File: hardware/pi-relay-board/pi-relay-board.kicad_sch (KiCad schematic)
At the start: 1 part, among them J1 Raspberry_Pi_2_3

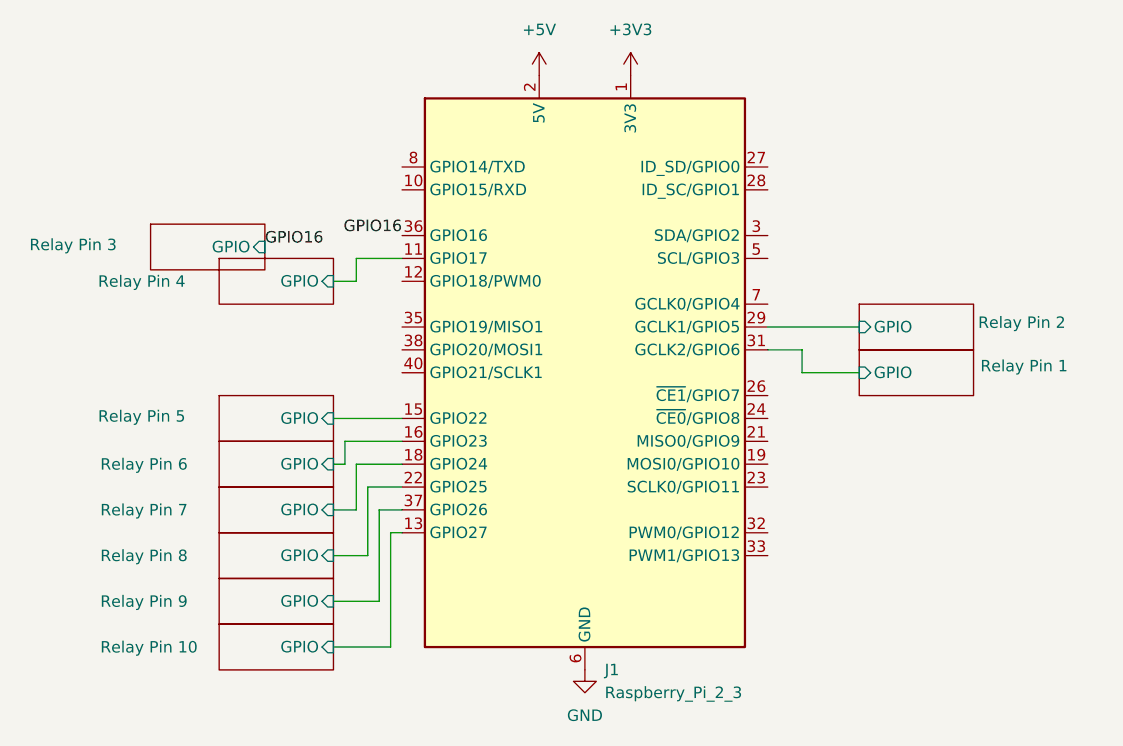
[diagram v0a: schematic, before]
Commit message: hardware: change to tht
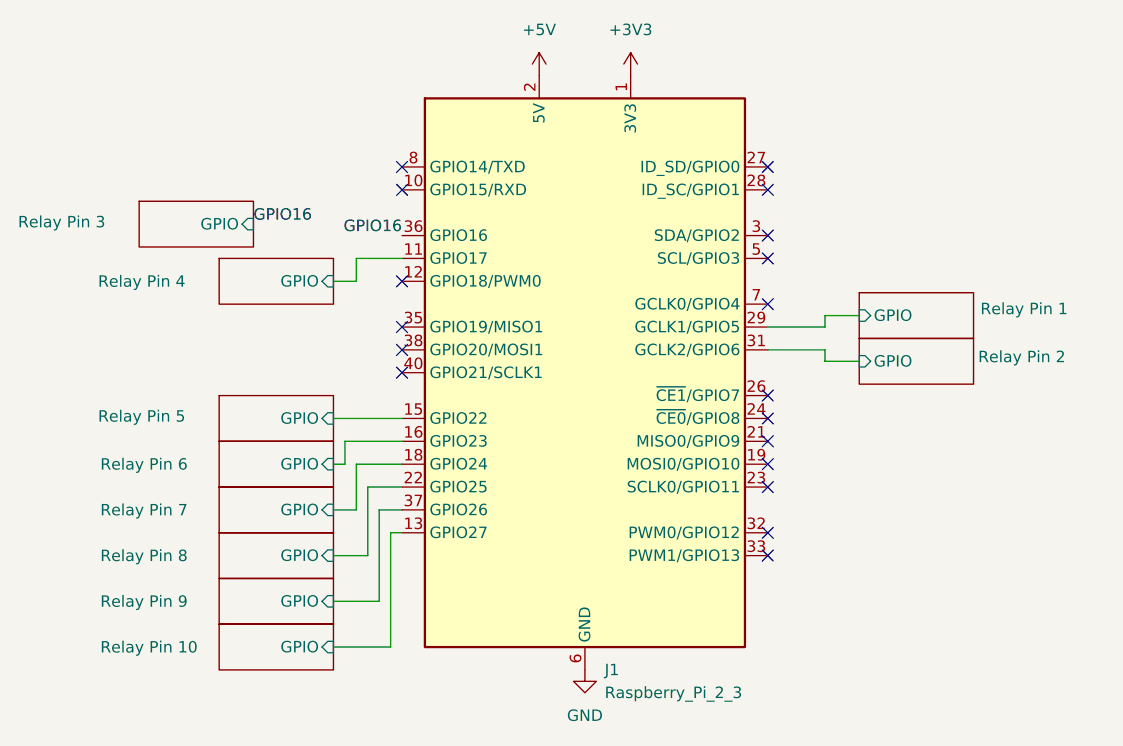
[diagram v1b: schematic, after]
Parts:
- J1: footprint custom:Raspberry Connector -> Connector_PinHeader_2.54mm:PinHeader_2x20_P2.54mm_Vertical
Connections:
- net Relay Pin 1/GPIO: now also J1.29 (GCLK1/GPIO5); no longer J1.31 (GCLK2/GPIO6)
- net Relay Pin 2/GPIO: now also J1.31 (GCLK2/GPIO6); no longer J1.29 (GCLK1/GPIO5)
- no-connect marks 0 -> 18
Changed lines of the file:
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@@
 	(generator_version "8.0")
 	(paper "A4")
+	(no_connect
+		(at 73.66 88.9)
+	)
+	(no_connect
+		(at 114.3 68.58)
+	)
+	(no_connect
+		(at 114.3 78.74)
+	)
+	(no_connect
+		(at 114.3 109.22)
+	)
+	(no_connect
+		(at 73.66 71.12)
+	)
+	(no_connect
+		(at 114.3 104.14)
+	)
+	(no_connect
+		(at 114.3 83.82)
+	)
+	(no_connect
+		(at 73.66 91.44)
+	)
+	(no_connect
+		(at 114.3 76.2)
+	)
+	(no_connect
+		(at 114.3 101.6)
+	)
+	(no_connect
+		(at 73.66 68.58)
+	)
+	(no_connect
+		(at 73.66 81.28)
+	)
+	(no_connect
+		(at 114.3 111.76)
+	)
+	(no_connect
+		(at 114.3 99.06)
+	)
+	(no_connect
+		(at 114.3 96.52)
+	)
+	(no_connect
+		(at 114.3 93.98)
+	)
+	(no_connect
+		(at 73.66 86.36)
+	)
+	(no_connect
+		(at 114.3 71.12)
+	)
 	(wire
 		(pts
@@
 	(wire
 		(pts
-			(xy 118.11 88.9) (xy 114.3 88.9)
+			(xy 120.65 88.9) (xy 120.65 90.17)
+		)
+		(stroke
+			(width 0)
+			(type default)
+		)
+	)
+	(wire
+		(pts
+			(xy 120.65 86.36) (xy 120.65 85.09)
 		)
 		(stroke
@@
 	(wire
 		(pts
-			(xy 124.46 91.44) (xy 118.11 91.44)
-		)
-		(stroke
-			(width 0)
-			(type default)
-		)
-	)
-	(wire
-		(pts
 			(xy 72.39 121.92) (xy 72.39 109.22)
 		)
@@
 	(wire
 		(pts
+			(xy 120.65 85.09) (xy 124.46 85.09)
+		)
+		(stroke
+			(width 0)
+			(type default)
+		)
+	)
+	(wire
+		(pts
+			(xy 114.3 88.9) (xy 120.65 88.9)
+		)
+		(stroke
+			(width 0)
+			(type default)
+		)
+	)
+	(wire
+		(pts
 			(xy 68.58 81.28) (xy 68.58 78.74)
 		)
@@
 	(wire
 		(pts
+			(xy 114.3 86.36) (xy 120.65 86.36)
+		)
+		(stroke
+			(width 0)
+			(type default)
+		)
+	)
+	(wire
+		(pts
 			(xy 67.31 101.6) (xy 67.31 99.06)
 		)
@@
 	(wire
 		(pts
-			(xy 114.3 86.36) (xy 124.46 86.36)
-		)
-		(stroke
-			(width 0)
-			(type default)
-		)
-	)
-	(wire
-		(pts
-			(xy 118.11 91.44) (xy 118.11 88.9)
+			(xy 120.65 90.17) (xy 124.46 90.17)
 		)
 		(stroke
@@
 	)
 	(label "GPIO16"
-		(at 58.42 77.47 0)
+		(at 57.15 74.93 0)
 		(fields_autoplaced yes)
 		(effects
@@
 			)
 		)
-		(property "Footprint" "custom:Raspberry Connector"
+		(property "Footprint" "Connector_PinHeader_2.54mm:PinHeader_2x20_P2.54mm_Vertical"
 			(at 93.98 91.44 0)
 			(effects
@@
 	)
 	(sheet
-		(at 45.72 74.93)
+		(at 44.45 72.39)
 		(size 12.7 5.08)
 		(stroke
@@
 		)
 		(property "Sheetname" "Relay Pin 3"
-			(at 32.258 77.978 0)
+			(at 30.988 75.438 0)
 			(effects
 				(font
@@
 		)
 		(property "Sheetfile" "relay_pin.kicad_sch"
-			(at 45.72 80.5946 0)
+			(at 44.45 78.0546 0)
 			(effects
 				(font
@@
 		)
 		(pin "GPIO" input
-			(at 58.42 77.47 0)
+			(at 57.15 74.93 0)
 			(effects
 				(font
@@
 	)
 	(sheet
-		(at 124.46 88.9)
+		(at 124.46 82.55)
 		(size 12.7 5.08)
 		(stroke
@@
 		)
 		(property "Sheetname" "Relay Pin 1"
-			(at 137.922 91.44 0)
+			(at 137.922 85.09 0)
 			(effects
 				(font
@@
 		)
 		(property "Sheetfile" "relay_pin.kicad_sch"
-			(at 124.46 94.5646 0)
+			(at 124.46 88.2146 0)
 			(effects
 				(font
@@
 		)
 		(pin "GPIO" input
-			(at 124.46 91.44 180)
+			(at 124.46 85.09 180)
 			(effects
 				(font
@@
 	)
 	(sheet
-		(at 124.46 83.82)
+		(at 124.46 87.63)
 		(size 12.7 5.08)
 		(stroke
@@
 		)
 		(property "Sheetname" "Relay Pin 2"
-			(at 137.668 86.614 0)
+			(at 137.668 90.424 0)
 			(effects
 				(font
@@
 		)
 		(property "Sheetfile" "relay_pin.kicad_sch"
-			(at 124.46 89.4846 0)
+			(at 124.46 93.2946 0)
 			(effects
 				(font
@@
 		)
 		(pin "GPIO" input
-			(at 124.46 86.36 180)
-			(effects
-				(font
+			(at 124.46 90.17 180)
+			(effects
+				(font

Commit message: feat: pcb bc547 footprint, laser image
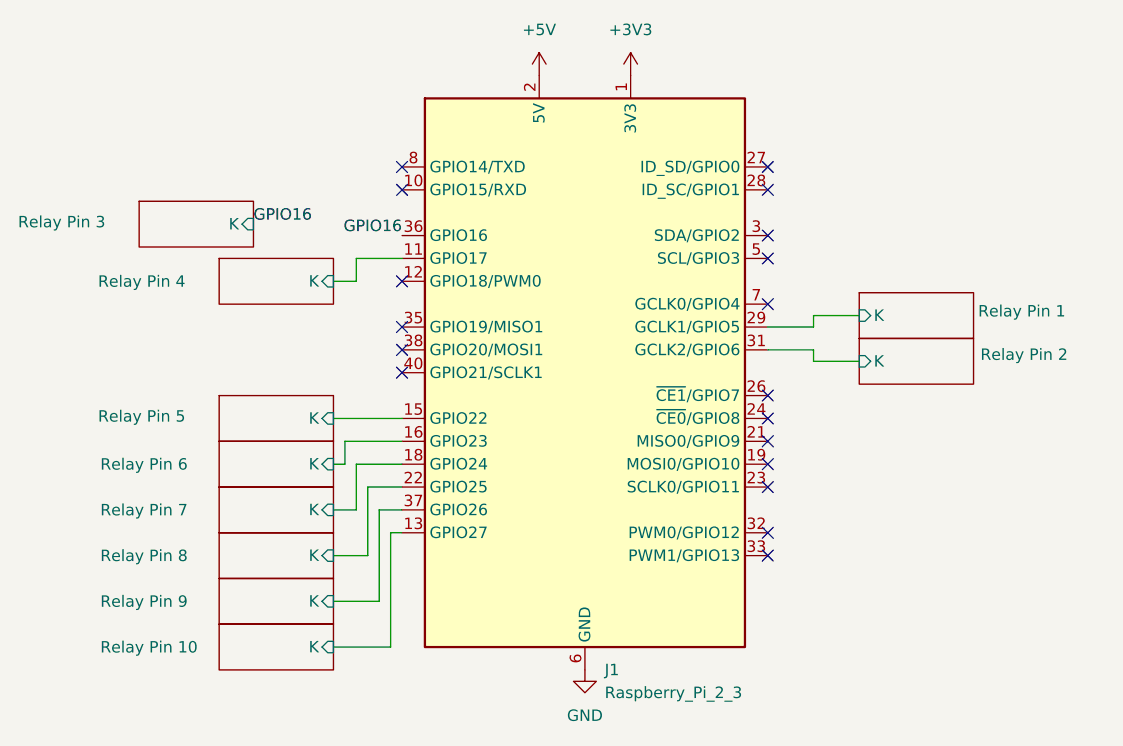
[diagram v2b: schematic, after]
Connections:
- net Relay Pin 1/GPIO renamed Relay Pin 1/K
- net Relay Pin 10/GPIO renamed Relay Pin 10/K
- net Relay Pin 2/GPIO renamed Relay Pin 2/K
- net Relay Pin 4/GPIO renamed Relay Pin 4/K
- net Relay Pin 5/GPIO renamed Relay Pin 5/K
- net Relay Pin 6/GPIO renamed Relay Pin 6/K
- net Relay Pin 7/GPIO renamed Relay Pin 7/K
- net Relay Pin 8/GPIO renamed Relay Pin 8/K
- net Relay Pin 9/GPIO renamed Relay Pin 9/K
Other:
- sheet Relay Pin 1 ports: added K; removed GPIO
- sheet Relay Pin 10 ports: added K; removed GPIO
- sheet Relay Pin 2 ports: added K; removed GPIO
- sheet Relay Pin 3 ports: added K; removed GPIO
- sheet Relay Pin 4 ports: added K; removed GPIO
- sheet Relay Pin 5 ports: added K; removed GPIO
- sheet Relay Pin 6 ports: added K; removed GPIO
- sheet Relay Pin 7 ports: added K; removed GPIO
- sheet Relay Pin 8 ports: added K; removed GPIO
- sheet Relay Pin 9 ports: added K; removed GPIO
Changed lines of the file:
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@@
 	(wire
 		(pts
-			(xy 120.65 88.9) (xy 120.65 90.17)
-		)
-		(stroke
-			(width 0)
-			(type default)
-		)
-	)
-	(wire
-		(pts
-			(xy 120.65 86.36) (xy 120.65 85.09)
+			(xy 119.38 88.9) (xy 119.38 90.17)
 		)
 		(stroke
@@
 	(wire
 		(pts
+			(xy 119.38 85.09) (xy 124.46 85.09)
+		)
+		(stroke
+			(width 0)
+			(type default)
+		)
+	)
+	(wire
+		(pts
 			(xy 72.39 121.92) (xy 72.39 109.22)
 		)
@@
 	(wire
 		(pts
-			(xy 120.65 85.09) (xy 124.46 85.09)
-		)
-		(stroke
-			(width 0)
-			(type default)
-		)
-	)
-	(wire
-		(pts
-			(xy 114.3 88.9) (xy 120.65 88.9)
+			(xy 119.38 86.36) (xy 114.3 86.36)
+		)
+		(stroke
+			(width 0)
+			(type default)
+		)
+	)
+	(wire
+		(pts
+			(xy 119.38 85.09) (xy 119.38 86.36)
 		)
 		(stroke
@@
 	(wire
 		(pts
-			(xy 114.3 86.36) (xy 120.65 86.36)
-		)
-		(stroke
-			(width 0)
-			(type default)
-		)
-	)
-	(wire
-		(pts
 			(xy 67.31 101.6) (xy 67.31 99.06)
 		)
@@
 	(wire
 		(pts
-			(xy 120.65 90.17) (xy 124.46 90.17)
+			(xy 114.3 88.9) (xy 119.38 88.9)
 		)
 		(stroke
@@
 		(pts
 			(xy 66.04 116.84) (xy 71.12 116.84)
+		)
+		(stroke
+			(width 0)
+			(type default)
+		)
+	)
+	(wire
+		(pts
+			(xy 119.38 90.17) (xy 124.46 90.17)
 		)
 		(stroke
@@
 			)
 		)
-		(pin "GPIO" input
+		(pin "K" input
 			(at 66.04 106.68 0)
 			(effects
@@
 			)
 		)
-		(pin "GPIO" input
+		(pin "K" input
 			(at 66.04 101.6 0)
 			(effects
@@
 			)
 		)
-		(pin "GPIO" input
+		(pin "K" input
 			(at 57.15 74.93 0)
 			(effects
@@
 			)
 		)
-		(pin "GPIO" input
+		(pin "K" input
 			(at 66.04 81.28 0)
 			(effects
@@
 			)
 		)
-		(pin "GPIO" input
+		(pin "K" input
 			(at 66.04 96.52 0)
 			(effects
@@
 				(path "/d2fef91f-5840-4773-b01e-415a95bac3ff"
 					(page "6")
+				)
+			)
+		)
+	)
+	(sheet
+		(at 124.46 87.63)
+		(size 12.7 5.08)
+		(stroke
+			(width 0.1524)
+			(type solid)
+		)
+		(fill
+			(color 0 0 0 0.0000)
+		)
+		(property "Sheetname" "Relay Pin 2"
+			(at 137.922 90.17 0)
+			(effects
+				(font
+					(size 1.27 1.27)
+				)
+				(justify left bottom)
+			)
+		)
+		(property "Sheetfile" "relay_pin.kicad_sch"
+			(at 124.46 93.2946 0)
+			(effects
+				(font
+					(size 1.27 1.27)
+				)
+				(justify left top)
+				(hide yes)
+			)
+		)
+		(pin "K" input
+			(at 124.46 90.17 180)
+			(effects
+				(font
+					(size 1.27 1.27)
+				)
+				(justify left)
+			)
+		)
+		(instances
+			(project "pi-relay-board"
+				(path "/d2fef91f-5840-4773-b01e-415a95bac3ff"
+					(page "2")
+				)
+			)
+		)
+	)
+	(sheet
+		(at 53.34 114.3)
+		(size 12.7 5.08)
+		(stroke
+			(width 0.1524)
+			(type solid)
+		)
+		(fill
+			(color 0 0 0 0.0000)
+		)
+		(property "Sheetname" "Relay Pin 9"
+			(at 40.132 117.602 0)
+			(effects
+				(font
+					(size 1.27 1.27)
+				)
+				(justify left bottom)
+			)
+		)
+		(property "Sheetfile" "relay_pin.kicad_sch"
+			(at 53.34 119.9646 0)
+			(effects
+				(font
+					(size 1.27 1.27)
+				)
+				(justify left top)
+				(hide yes)
+			)
+		)
+		(pin "K" input
+			(at 66.04 116.84 0)
+			(effects
+				(font
+					(size 1.27 1.27)
+				)
+				(justify right)
+			)
+		)
+		(instances
+			(project "pi-relay-board"
+				(path "/d2fef91f-5840-4773-b01e-415a95bac3ff"
+					(page "10")
+				)
+			)
+		)
+	)
+	(sheet
+		(at 53.34 109.22)
+		(size 12.7 5.08)
+		(stroke
+			(width 0.1524)
+			(type solid)
+		)
+		(fill
+			(color 0 0 0 0.0000)
+		)
+		(property "Sheetname" "Relay Pin 8"
+			(at 40.132 112.522 0)
+			(effects
+				(font
+					(size 1.27 1.27)
+				)
+				(justify left bottom)
+			)
+		)
+		(property "Sheetfile" "relay_pin.kicad_sch"
+			(at 53.34 114.8846 0)
+			(effects
+				(font
+					(size 1.27 1.27)
+				)
+				(justify left top)
+				(hide yes)
+			)
+		)
+		(pin "K" input
+			(at 66.04 111.76 0)
+			(effects
+				(font
+					(size 1.27 1.27)
+				)
+				(justify right)
+			)
+		)
+		(instances
+			(project "pi-relay-board"
+				(path "/d2fef91f-5840-4773-b01e-415a95bac3ff"
+					(page "9")
 				)
 			)
@@
 		)
 		(property "Sheetname" "Relay Pin 1"
-			(at 137.922 85.09 0)
+			(at 137.668 85.344 0)
 			(effects
 				(font
@@
 			)
 		)
-		(pin "GPIO" input
+		(pin "K" input
 			(at 124.46 85.09 180)
-			(effects
-				(font
-					(size 1.27 1.27)
-				)
-				(justify left)
-			)
-		)
-		(instances
-			(project "pi-relay-board"
-				(path "/d2fef91f-5840-4773-b01e-415a95bac3ff"
-					(page "2")
-				)
-			)
-		)
-	)
-	(sheet
-		(at 53.34 114.3)
-		(size 12.7 5.08)
-		(stroke
-			(width 0.1524)
-			(type solid)
-		)
-		(fill
-			(color 0 0 0 0.0000)
-		)
-		(property "Sheetname" "Relay Pin 9"
-			(at 40.132 117.602 0)
-			(effects
-				(font
-					(size 1.27 1.27)
-				)
-				(justify left bottom)
-			)
-		)
-		(property "Sheetfile" "relay_pin.kicad_sch"
-			(at 53.34 119.9646 0)
-			(effects
-				(font
-					(size 1.27 1.27)
-				)
-				(justify left top)
-				(hide yes)
-			)
-		)
-		(pin "GPIO" input
-			(at 66.04 116.84 0)
-			(effects
-				(font
-					(size 1.27 1.27)
-				)
-				(justify right)
-			)
-		)
-		(instances
-			(project "pi-relay-board"
-				(path "/d2fef91f-5840-4773-b01e-415a95bac3ff"
-					(page "10")
-				)
-			)
-		)
-	)
-	(sheet
-		(at 53.34 109.22)
-		(size 12.7 5.08)
-		(stroke
-			(width 0.1524)
-			(type solid)
-		)
-		(fill
-			(color 0 0 0 0.0000)
-		)
-		(property "Sheetname" "Relay Pin 8"
-			(at 40.132 112.522 0)
-			(effects
-				(font
-					(size 1.27 1.27)
-				)
-				(justify left bottom)
-			)
-		)
-		(property "Sheetfile" "relay_pin.kicad_sch"
-			(at 53.34 114.8846 0)
-			(effects
-				(font
-					(size 1.27 1.27)
-				)
-				(justify left top)
-				(hide yes)
-			)
-		)
-		(pin "GPIO" input
-			(at 66.04 111.76 0)
-			(effects
-				(font
-					(size 1.27 1.27)
-				)
-				(justify right)
-			)
-		)
-		(instances
-			(project "pi-relay-board"
-				(path "/d2fef91f-5840-4773-b01e-415a95bac3ff"
-					(page "9")
-				)
-			)
-		)
-	)
-	(sheet
-		(at 124.46 87.63)
-		(size 12.7 5.08)
-		(stroke
-			(width 0.1524)
-			(type solid)
-		)
-		(fill
-			(color 0 0 0 0.0000)
-		)
-		(property "Sheetname" "Relay Pin 2"
-			(at 137.668 90.424 0)
-			(effects
-				(font
-					(size 1.27 1.27)
-				)
-				(justify left bottom)
-			)
-		)
-		(property "Sheetfile" "relay_pin.kicad_sch"
-			(at 124.46 93.2946 0)
-			(effects
-				(font
-					(size 1.27 1.27)
-				)
-				(justify left top)
-				(hide yes)
-			)
-		)
-		(pin "GPIO" input
-			(at 124.46 90.17 180)
 			(effects
 				(font
@@
 			)
 		)
-		(pin "GPIO" input
+		(pin "K" input
 			(at 66.04 121.92 0)
 			(effects
